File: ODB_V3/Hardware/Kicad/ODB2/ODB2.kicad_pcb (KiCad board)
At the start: 6 copper layers, 63.5 x 123.1 mm, 238 parts, among them IC1 W25Q512JVEIQ, J1 1715310000, J10 GPS_Conn_02x04_Top_Bottom, J15 Vin_XT30PW-F, J2 RFD_GT17HN-4DP-2HA56, J3 SYS_SW_Conn_01x05_Header, J5 MEM2067, J6 IdeFIX_GT17HN-4DP-2HA56, J7 1715250000, J8 1715310000, J9 1715250000, U1 STM32F412ZGTx, U10 ADXL382-2BCCZ-RL7, U11 SI5442DU-T1-GE3, U12 SI5442DU-T1-GE3, U13 L6981N33DR, U2 LM339, U3 SI5442DU-T1-GE3, U4 MS580301BA01-00, U6 BNO055, U7 MPQ9843GLE-5-AEC1-Z, U8 SI5442DU-T1-GE3, U9 MAX6612MXK, Y1 ABM8G-25.000MHZ-18-D2Y-T

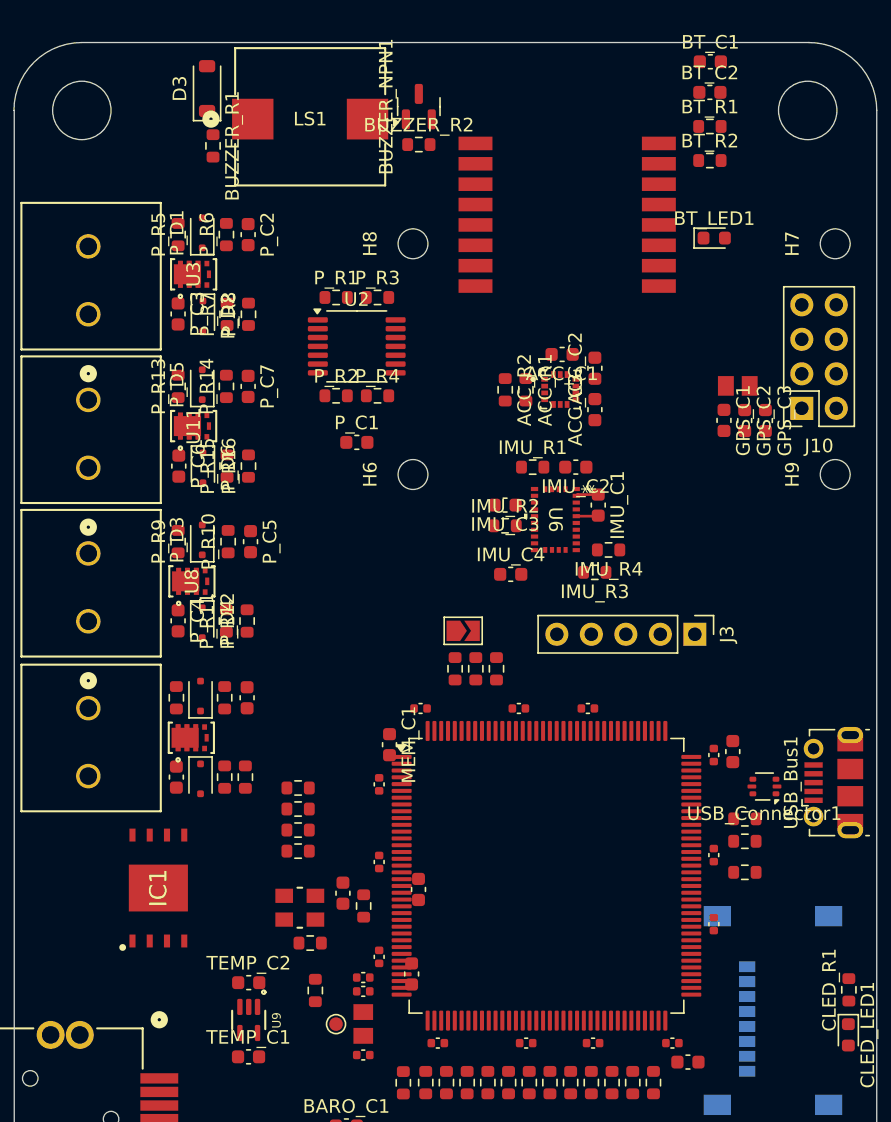
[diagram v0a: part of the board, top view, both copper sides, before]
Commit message: fix: hm11 + add GND  jumper to RESETB pullup
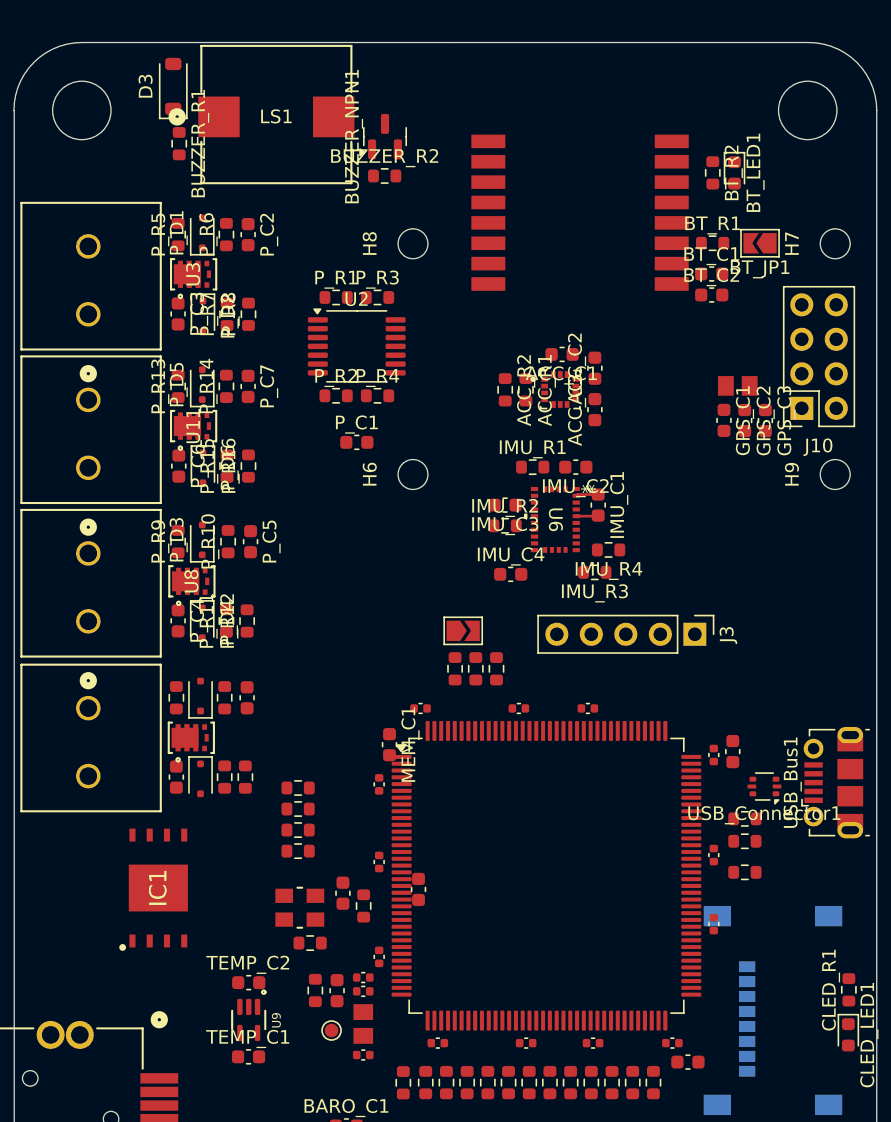
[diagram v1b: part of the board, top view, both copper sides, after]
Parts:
- added BT_JP1: SolderJumper_2_Open, Jumper:SolderJumper-2_P1.3mm_Open_TrianglePad1.0x1.5mm, F.Cu at (171.9, 47.8)
- moved BT_C1 15.6 mm to (168.4, 50.0)
- moved BT_C2 14.9 mm to (168.4, 51.6)
- moved BT_R1 8.60 mm to (168.4, 47.8)
- moved RST_C1 5.62 mm to (140.8, 102.8)
- moved BT_LED1 5.03 mm to (170.1, 42.6), turned to -90 degrees
- moved BUZZER_R2 3.42 mm to (144.3, 42.8)
- moved BUZZER_NPN1 3.33 mm to (144.3, 39.9)
- moved LS1 2.49 mm to (136.3, 38.3)
- moved BUZZER_R1 2.49 mm to (129.2, 40.4)
- moved D3 2.49 mm to (128.7, 36.2)
- moved H5 0.96 mm to (158.4, 43.3)
- moved BT_R2 0.93 mm to (168.5, 42.6), turned to -90 degrees
- moved TP1 0.57 mm to (140.4, 105.7)
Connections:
- BT_C1 pad 1: Net-(H5-GND) -> 3V3_Main
- BT_R1 pad 1: 3V3_Main -> Net-(BT_JP1-B)
- BT_R1 pad 2: Net-(H5-GND) -> 3V3_Main
- H5 pad 11: GND -> Net-(BT_JP1-B)
- H5 pad 12: Net-(H5-GND) -> GND
- U1 pad 59: unconnected-(U1-PE8-Pad59) -> Power_Good
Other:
- outline, holes or cut-outs redrawn

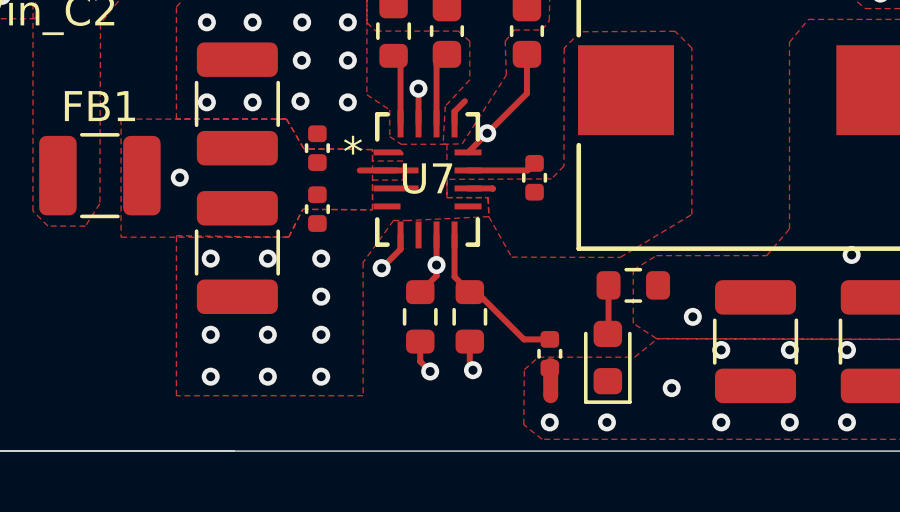
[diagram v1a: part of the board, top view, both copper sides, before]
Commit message: feat: add good power input to stm32 + add pull-up 3v3 to good power
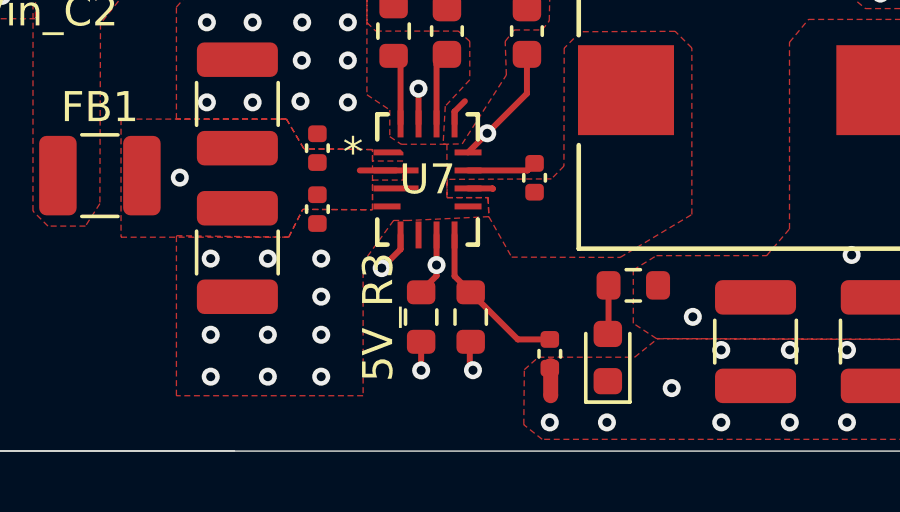
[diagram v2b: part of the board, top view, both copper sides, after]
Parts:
- 5V_R3: value 100k -> 10k
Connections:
- 5V_R3 pad 1: Net-(U7-VCC) -> 3V3_Main
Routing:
- net Net-(U7-VCC): track 13.9 -> 4.08 mm, vias 2 -> 1
- net 3V3_Main: track 1.66 -> 2.61 mm, vias 27 -> 28

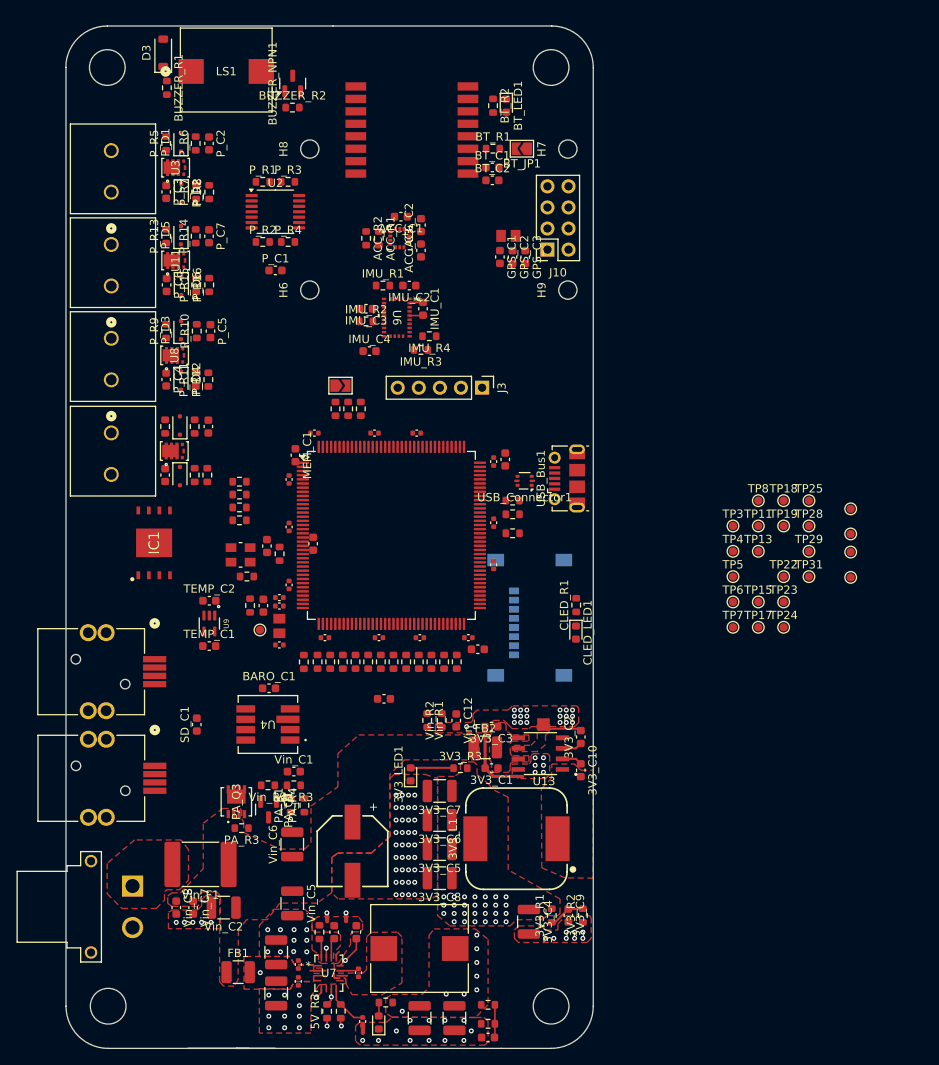
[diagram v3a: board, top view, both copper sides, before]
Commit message: WIP : Add GPIO extend, replace 5mm terminal with 2.54mm, densify layout
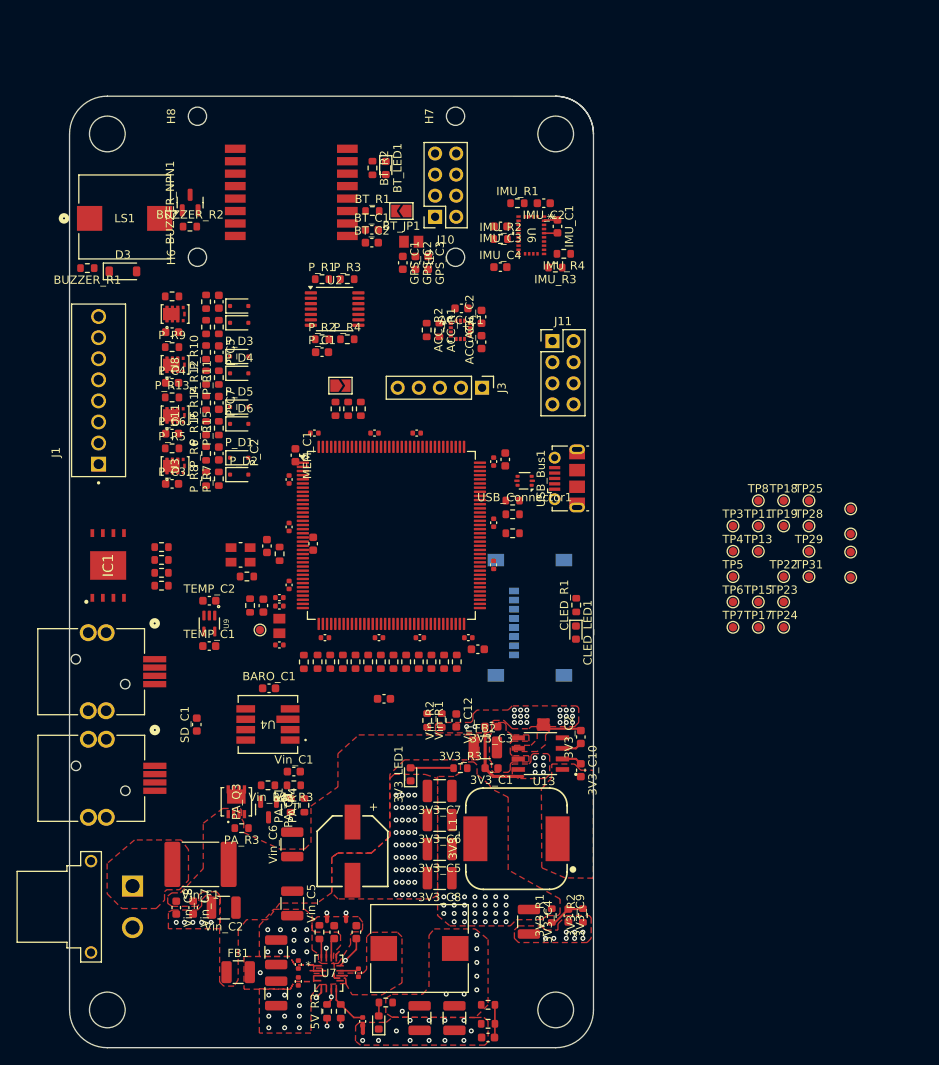
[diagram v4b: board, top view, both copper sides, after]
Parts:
- removed J7, J9: 1715250000, ODB:CONN_1715310000
- removed J8: 1715310000, ODB:CONN_1715310000
- added J11: Conn_02x04_Odd_Even, Connector_PinHeader_2.54mm:PinHeader_2x04_P2.54mm_Vertical, F.Cu at (175.6, 71.0)
- J1: value 1715310000 -> Screw_Terminal_01x08; footprint ODB:CONN_1715310000 -> ODB:8pin_terminal_2mm54
- moved P_D1 38.6 mm to (137.9, 85.0), turned to 0 degrees
- moved P_R6 37.4 mm to (133.9, 84.5)
- moved P_C2 37.4 mm to (135.4, 84.5)
- moved P_R5 36.7 mm to (129.8, 83.9), turned to 0 degrees
- moved U3 35.9 mm to (130.2, 86.0)
- moved P_C3 35.2 mm to (129.8, 88.1), turned to 0 degrees
- moved P_R7 34.6 mm to (135.4, 87.5)
- moved P_D2 34.6 mm to (137.9, 87.0), turned to 0 degrees
- moved P_R8 34.5 mm to (133.9, 87.5)
- moved D3 26.8 mm to (123.9, 62.6), turned to 0 degrees
- moved J1 23.9 mm to (120.9, 76.9)
- moved BUZZER_R1 23.7 mm to (119.6, 62.2), turned to 180 degrees
- moved P_D5 21.9 mm to (137.9, 78.9), turned to 0 degrees
- moved LS1 21.5 mm to (124.1, 56.0)
- moved P_R14 20.1 mm to (133.9, 78.4)
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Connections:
- net Net-(J1-Pad2) renamed Pryo1-
- J1 pad 1: Vin_Pyro -> Pryo1+
- PA_Q3 pad 5: Vin_Pyro -> Pryo1+
- PA_Q3 pad 6: Vin_Pyro -> Pryo1+
- PA_Q3 pad 7: Vin_Pyro -> Pryo1+
- PA_Q3 pad 8: Vin_Pyro -> Pryo1+
- P_C3 pad 1: Vin_Pyro -> Pryo1+
- P_C4 pad 1: Vin_Pyro -> Pryo1+
- P_C6 pad 1: Vin_Pyro -> Pryo1+
- P_C8 pad 1: Vin_Pyro -> Pryo1+
- P_R13 pad 1: Net-(J8-Pad2) -> Pryo2-
- P_R17 pad 1: Net-(J9-Pad2) -> Pryo4-
- P_R9 pad 1: Net-(J7-Pad2) -> Pryo3-
- U11 pad 1: Net-(J8-Pad2) -> Pryo2-
- U11 pad 2: Net-(J8-Pad2) -> Pryo2-
- U11 pad 3: Net-(J8-Pad2) -> Pryo2-
- U11 pad 6: Net-(J8-Pad2) -> Pryo2-
- U11 pad 7: Net-(J8-Pad2) -> Pryo2-
- U11 pad 8: Net-(J8-Pad2) -> Pryo2-
- U12 pad 1: Net-(J9-Pad2) -> Pryo4-
- U12 pad 2: Net-(J9-Pad2) -> Pryo4-
- U12 pad 3: Net-(J9-Pad2) -> Pryo4-
- U12 pad 6: Net-(J9-Pad2) -> Pryo4-
- U12 pad 7: Net-(J9-Pad2) -> Pryo4-
- U12 pad 8: Net-(J9-Pad2) -> Pryo4-
- U8 pad 1: Net-(J7-Pad2) -> Pryo3-
- U8 pad 2: Net-(J7-Pad2) -> Pryo3-
- U8 pad 3: Net-(J7-Pad2) -> Pryo3-
- U8 pad 6: Net-(J7-Pad2) -> Pryo3-
- U8 pad 7: Net-(J7-Pad2) -> Pryo3-
- U8 pad 8: Net-(J7-Pad2) -> Pryo3-
- Vin_R4 pad 2: Vin_Pyro -> Pryo1+
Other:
- board size 63.5 x 123.1 mm -> 63.1 x 114.6 mm

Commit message: WIP : Pyro powerplane couche dessus
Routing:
- net Pryo1+: vias 0 -> 10
- added copper zone on F.Cu, net Pryo1+
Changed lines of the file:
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@@
 		(net 22)
+	)
+	(via
+		(at 135.581841 122.445511)
+		(size 0.6)
+		(drill 0.3)
+		(layers "F.Cu" "B.Cu")
+		(free yes)
+		(net 261)
+	)
+	(via
+		(at 139.521248 122.445511)
+		(size 0.6)
+		(drill 0.3)
+		(layers "F.Cu" "B.Cu")
+		(free yes)
+		(net 261)
+	)
+	(via
+		(at 138.536396 122.445511)
+		(size 0.6)
+		(drill 0.3)
+		(layers "F.Cu" "B.Cu")
+		(free yes)
+		(net 261)
+	)
+	(via
+		(at 135.569492 123.297608)
+		(size 0.6)
+		(drill 0.3)
+		(layers "F.Cu" "B.Cu")
+		(free yes)
+		(net 261)
+	)
+	(via
+		(at 137.551545 122.445511)
+		(size 0.6)
+		(drill 0.3)
+		(layers "F.Cu" "B.Cu")
+		(free yes)
+		(net 261)
+	)
+	(via
+		(at 136.557431 123.297608)
+		(size 0.6)
+		(drill 0.3)
+		(layers "F.Cu" "B.Cu")
+		(free yes)
+		(net 261)
+	)
+	(via
+		(at 137.54537 123.297608)
+		(size 0.6)
+		(drill 0.3)
+		(layers "F.Cu" "B.Cu")
+		(free yes)
+		(net 261)
+	)
+	(via
+		(at 138.533309 123.297608)
+		(size 0.6)
+		(drill 0.3)
+		(layers "F.Cu" "B.Cu")
+		(free yes)
+		(net 261)
+	)
+	(via
+		(at 136.566693 122.445511)
+		(size 0.6)
+		(drill 0.3)
+		(layers "F.Cu" "B.Cu")
+		(free yes)
+		(net 261)
+	)
+	(via
+		(at 139.521248 123.297608)
+		(size 0.6)
+		(drill 0.3)
+		(layers "F.Cu" "B.Cu")
+		(free yes)
+		(net 261)
 	)
 	(zone
@@
 			)
 		)
+	)
+	(zone
+		(net 261)
+		(net_name "Pryo1+")
+		(layer "F.Cu")
+		(hatch edge 0.5)
+		(priority 18)
+		(connect_pads
+			(clearance 0.25)
+		)
+		(min_thickness 0.25)
+		(filled_areas_thickness no)
+		(fill yes
+			(thermal_gap 0.5)
+			(thermal_bridge_width 0.5)
+			(island_removal_mode 1)
+			(island_area_min 10)
+		)
+		(polygon
+			(pts
+				(xy 135.979865 126.6591) (xy 138.6556 126.6591) (xy 139.867824 125.385712) (xy 141.093667 125.385712)
+				(xy 141.349051 124.994123) (xy 141.351873 122.650476) (xy 139.989076 121.606186) (xy 135.794446 121.62988)
+				(xy 134.706391 122.427786) (xy 134.730257 125.267881)
+			)
+		)
